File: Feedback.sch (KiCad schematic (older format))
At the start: 1 part

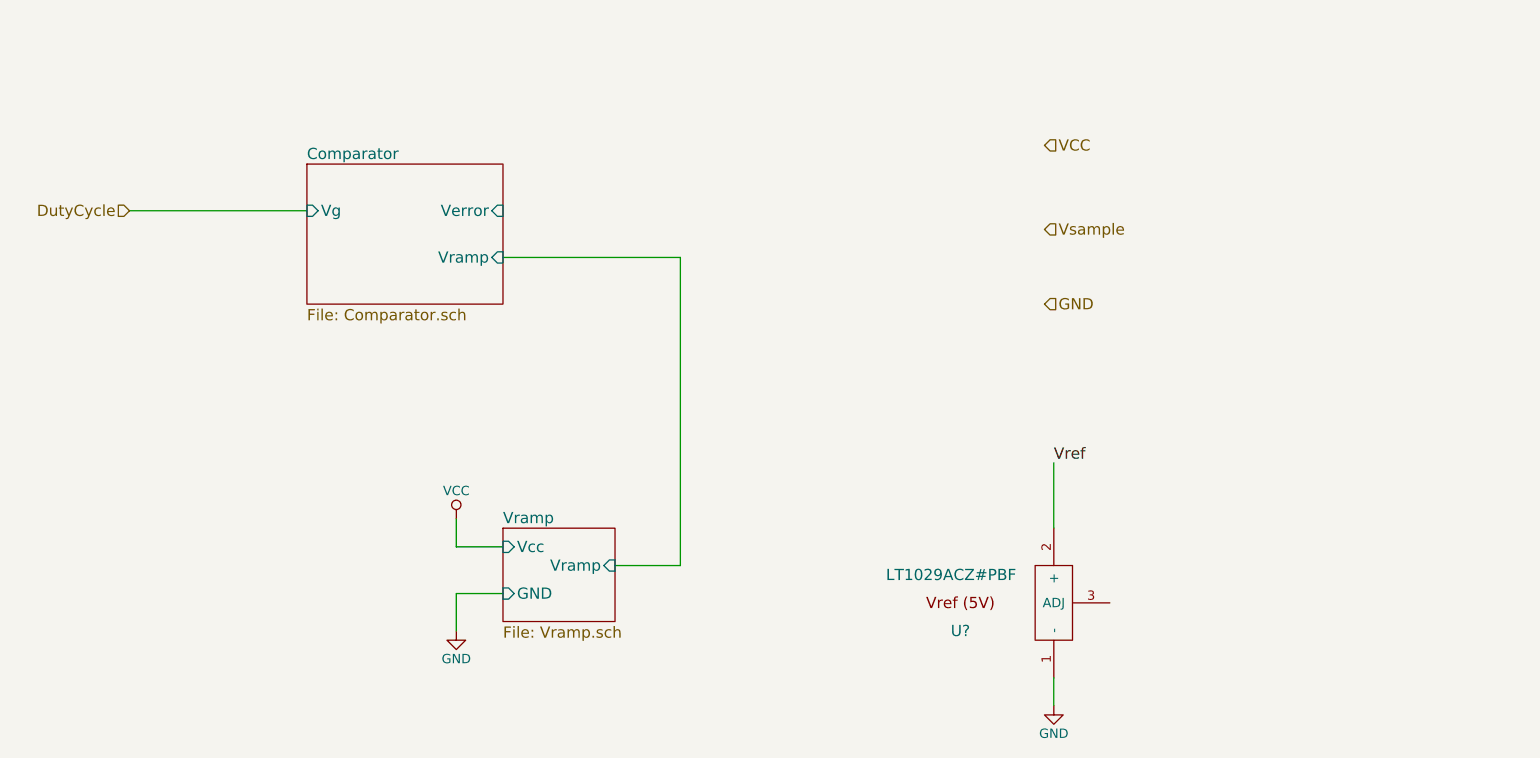
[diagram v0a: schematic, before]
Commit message: Added the basic Buck Schematic with the IRL2004
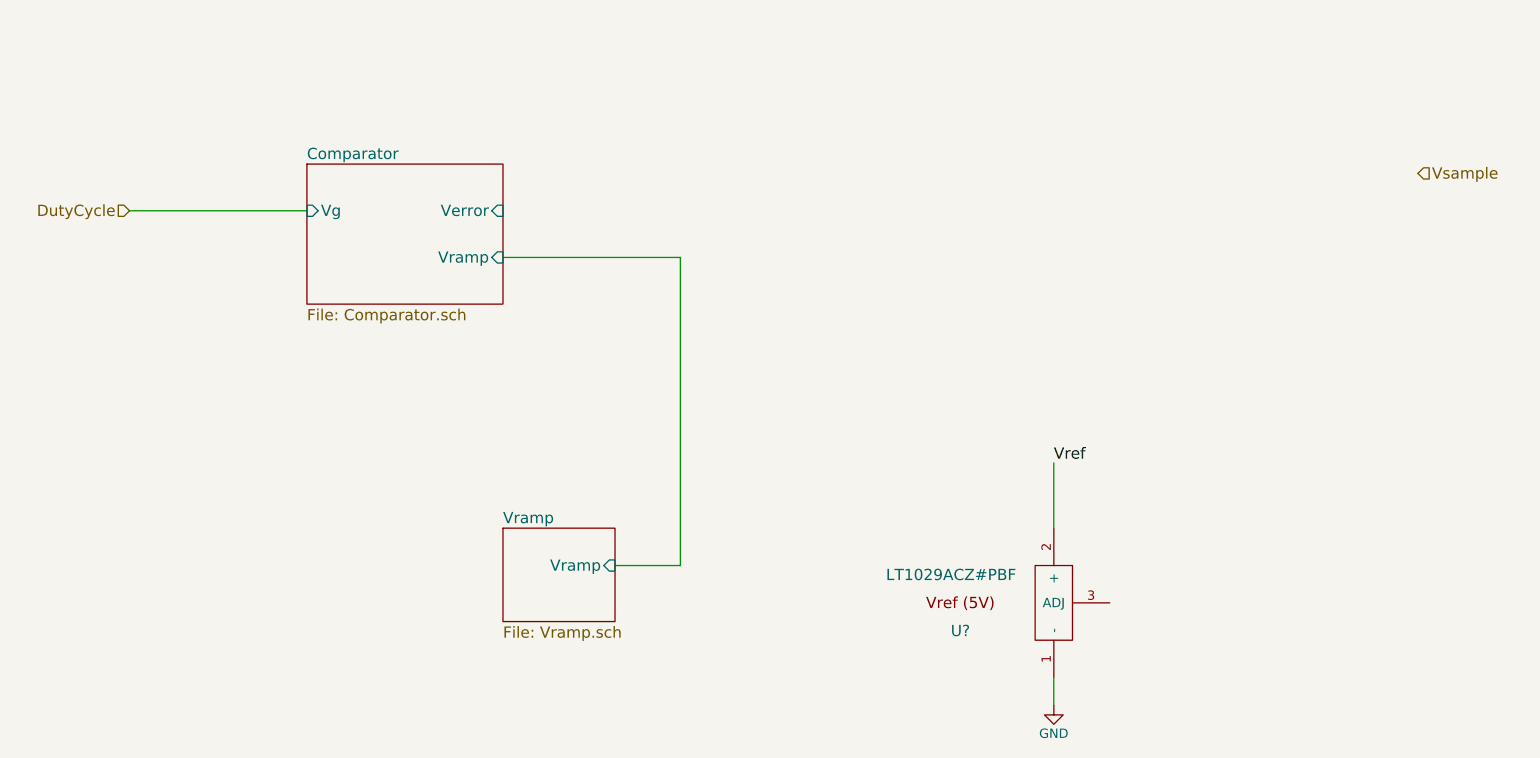
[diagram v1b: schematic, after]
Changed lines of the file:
@@
 LIBS:valves
 LIBS:Buck Supply-cache
+LIBS:ir
 EELAYER 25 0
 EELAYER END
@@
 Comment4 ""
 $EndDescr
-Text HLabel 6900 2800 2    60   Input ~ 0
+Text HLabel 8900 2500 2    60   Input ~ 0
 Vsample
 Text HLabel 2000 2700 0    60   Input ~ 0
@@
 F0 "Vramp" 60
 F1 "Vramp.sch" 60
-F2 "Vcc" I L 4000 4500 60
-F3 "GND" I L 4000 4750 60
-F4 "Vramp" I R 4600 4600 60
+F2 "Vramp" I R 4600 4600 60
 $EndSheet
-$Comp
-L GND #PWR?
-U 1 1 58B66F61
-P 3750 4950
-F 0 "#PWR?" H 3750 4700 50  0001 C CNN
-F 1 "GND" H 3750 4800 50  0000 C CNN
-F 2 "" H 3750 4950 50  0000 C CNN
-F 3 "" H 3750 4950 50  0000 C CNN
-	1    3750 4950
-	1    0    0    -1
-$EndComp
-$Comp
-L VCC #PWR?
-U 1 1 58B66F95
-P 3750 4350
-F 0 "#PWR?" H 3750 4200 50  0001 C CNN
-F 1 "VCC" H 3750 4500 50  0000 C CNN
-F 2 "" H 3750 4350 50  0000 C CNN
-F 3 "" H 3750 4350 50  0000 C CNN
-	1    3750 4350
-	1    0    0    -1
-$EndComp
-Wire Wire Line
-	4000 4500 3750 4500
-Wire Wire Line
-	3750 4500 3750 4350
-Wire Wire Line
-	3750 4950 3750 4750
-Wire Wire Line
-	3750 4750 4000 4750
 Wire Wire Line
 	4000 2950 4950 2950
@@
 Wire Wire Line
 	4950 4600 4600 4600
-Text HLabel 6900 3200 2    60   Input ~ 0
-GND
-Text HLabel 6900 2350 2    60   Input ~ 0
-VCC
 $EndSCHEMATC

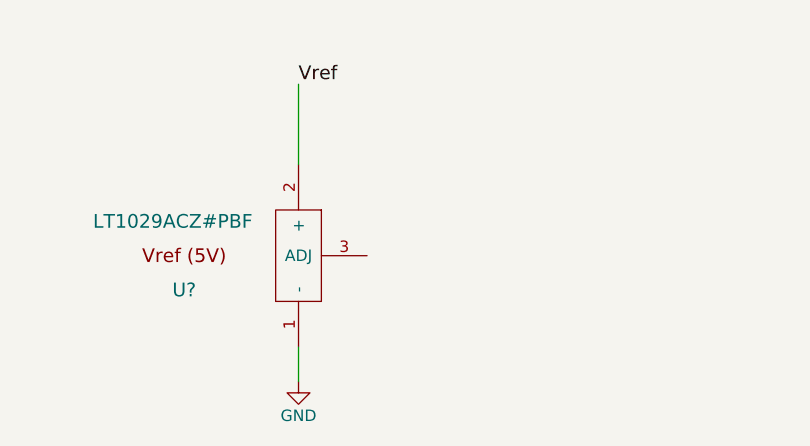
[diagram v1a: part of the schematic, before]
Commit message: Created Ramp Voltage Source
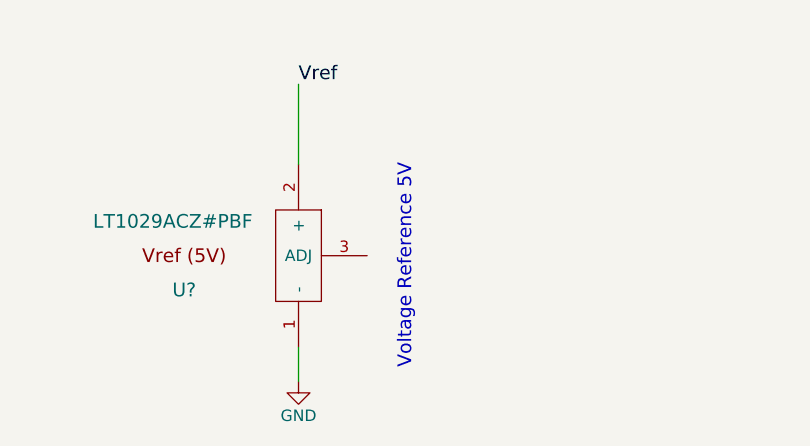
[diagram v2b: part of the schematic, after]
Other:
- note added: "Voltage Reference 5V\n"
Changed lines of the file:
@@
 Wire Wire Line
 	4950 4600 4600 4600
+Text Notes 7450 4400 3    60   ~ 0
+Voltage Reference 5V\n
 $EndSCHEMATC

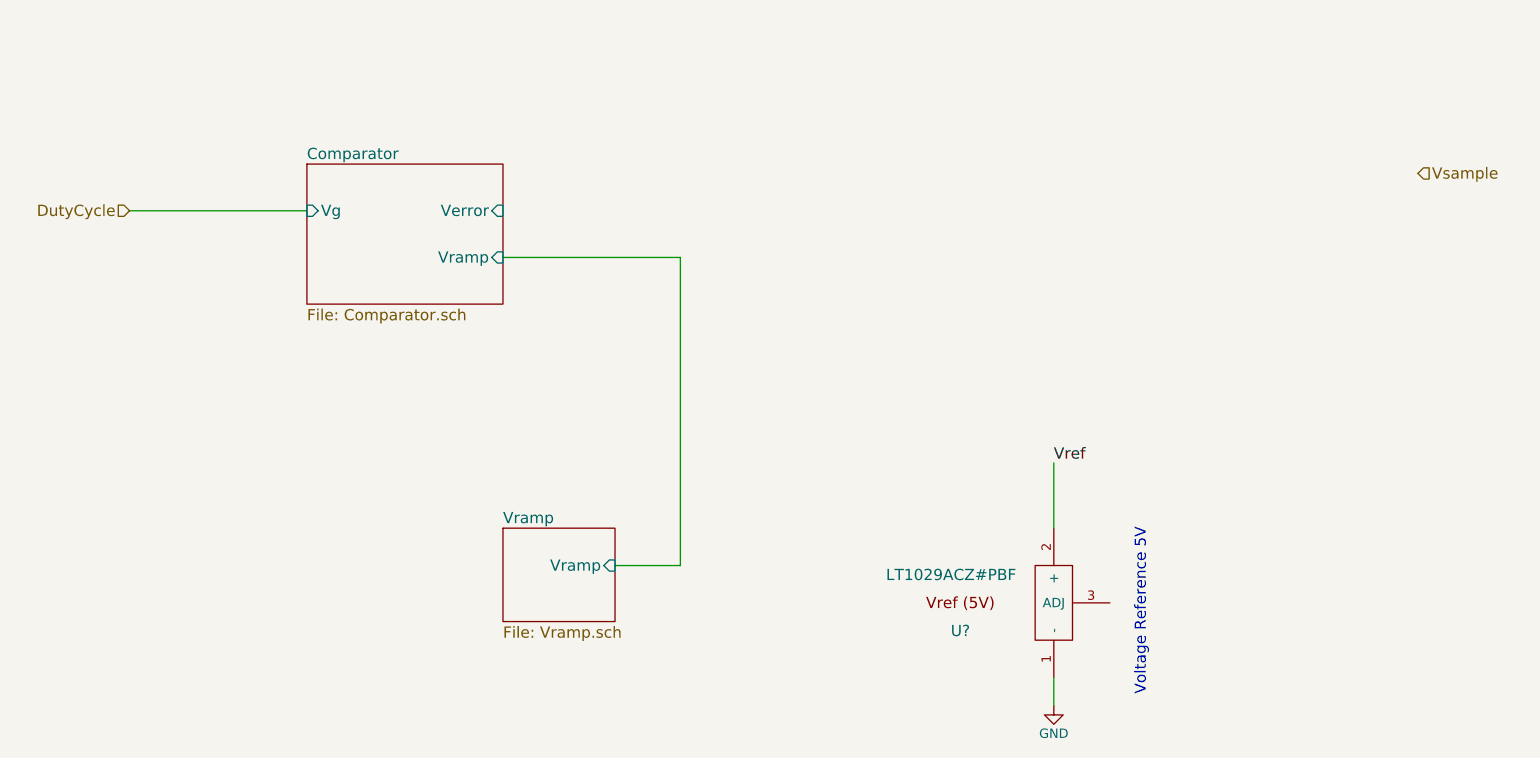
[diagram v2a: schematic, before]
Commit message: Finished the full circuit.
All thats left is to set the design parameters.
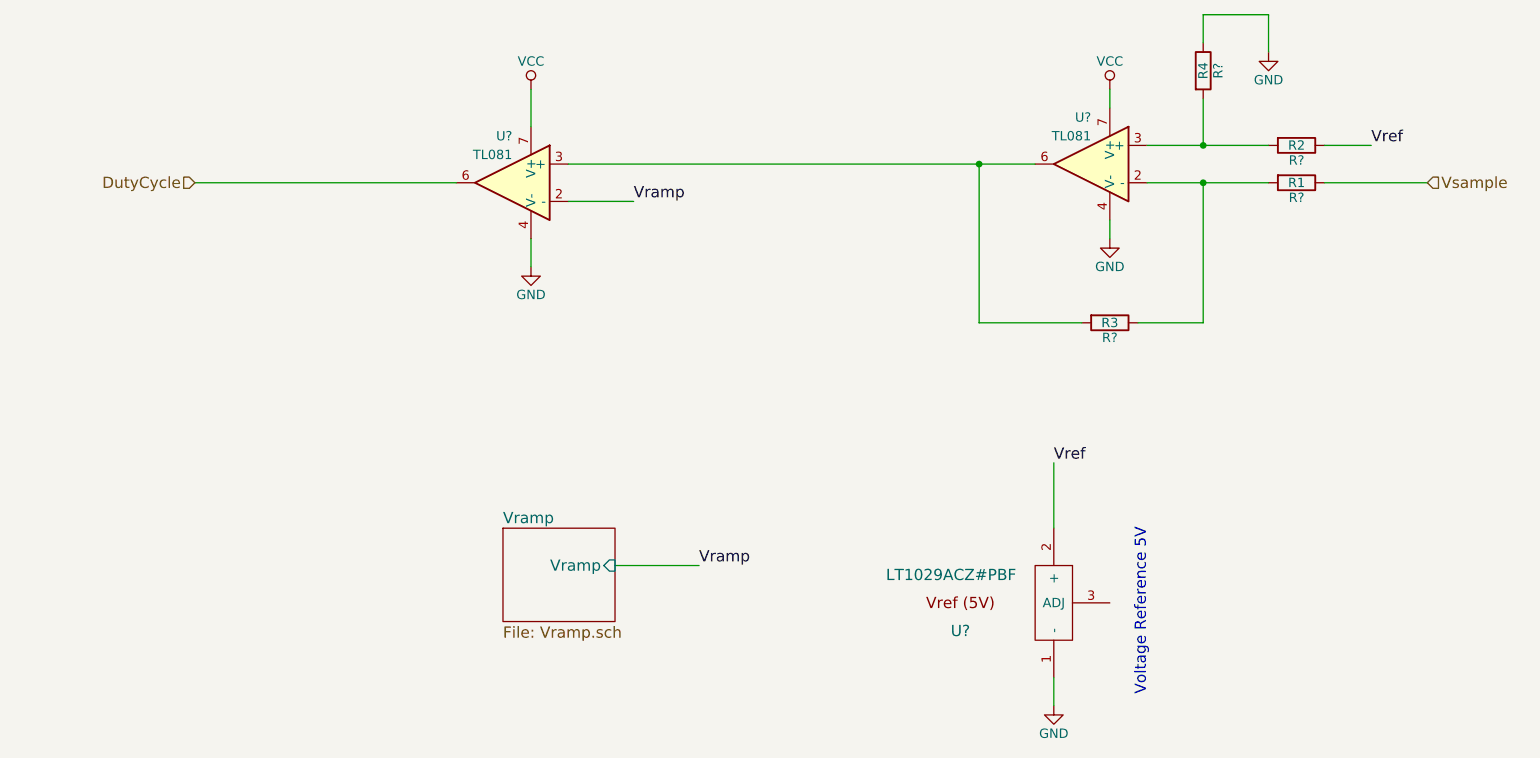
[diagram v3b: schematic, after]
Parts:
- added R?: R1, symbol R
- added R?: R3, symbol R
- added R?: R2, symbol R
- added R?: R4, symbol R
- added U? (x2): TL081, symbol TL081
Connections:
- net DutyCycle: now also U?.6
- net GND: now also R?.1, U?.4 (V-), U?.4 (V-)
- net Vref: now also R?.1
- net Vsample: now also R?.1
- new net: R?.1, R?.2, U?.2 (-)
- new net: R?.2, R?.2, U?.3 (+)
- new net: R?.2, U?.3 (+), U?.6
- new net VCC: U?.7 (V+), U?.7 (V+)
- new net Vramp: U?.2 (-)
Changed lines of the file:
@@
 $Descr A4 11693 8268
 encoding utf-8
-Sheet 2 5
+Sheet 2 4
 Title ""
 Date ""
@@
 Comment4 ""
 $EndDescr
-Text HLabel 8900 2500 2    60   Input ~ 0
+Text HLabel 8950 2550 2    60   Input ~ 0
 Vsample
-Text HLabel 2000 2700 0    60   Input ~ 0
+Text HLabel 2350 2550 0    60   Input ~ 0
 DutyCycle
-$Sheet
-S 2950 2450 1050 750
-U 58B64594
-F0 "Comparator" 60
-F1 "Comparator.sch" 60
-F2 "Vg" I L 2950 2700 60
-F3 "Verror" I R 4000 2700 60
-F4 "Vramp" I R 4000 2950 60
-$EndSheet
 $Comp
 L LT1029ACZ#PBF U?
@@
 Text Label 6950 4050 0    60   ~ 0
 Vref
-Wire Wire Line
-	2000 2700 2950 2700
 $Sheet
 S 4000 4400 600  500
@@
 F2 "Vramp" I R 4600 4600 60
 $EndSheet
-Wire Wire Line
-	4000 2950 4950 2950
-Wire Wire Line
-	4950 2950 4950 4600
-Wire Wire Line
-	4950 4600 4600 4600
 Text Notes 7450 4400 3    60   ~ 0
 Voltage Reference 5V\n
+$Comp
+L TL081 U?
+U 1 1 58B85FB5
+P 7150 2450
+F 0 "U?" H 7150 2700 50  0000 L CNN
+F 1 "TL081" H 7150 2600 50  0000 L CNN
+F 2 "" H 7200 2650 50  0000 C CNN
+F 3 "" H 7150 2700 50  0000 C CNN
+	1    7150 2450
+	-1   0    0    -1
+$EndComp
+Wire Wire Line
+	7450 2350 8100 2350
+Text Label 8650 2350 0    60   ~ 0
+Vref
+$Comp
+L GND #PWR?
+U 1 1 58B861EE
+P 7250 2850
+F 0 "#PWR?" H 7250 2600 50  0001 C CNN
+F 1 "GND" H 7250 2700 50  0000 C CNN
+F 2 "" H 7250 2850 50  0000 C CNN
+F 3 "" H 7250 2850 50  0000 C CNN
+	1    7250 2850
+	1    0    0    -1
+$EndComp
+Wire Wire Line
+	7250 2750 7250 2850
+$Comp
+L VCC #PWR?
+U 1 1 58B86218
+P 7250 2050
+F 0 "#PWR?" H 7250 1900 50  0001 C CNN
+F 1 "VCC" H 7250 2200 50  0000 C CNN
+F 2 "" H 7250 2050 50  0000 C CNN
+F 3 "" H 7250 2050 50  0000 C CNN
+	1    7250 2050
+	1    0    0    -1
+$EndComp
+Wire Wire Line
+	7250 2150 7250 2050
+$Comp
+L TL081 U?
+U 1 1 58B86315
+P 4050 2550
+F 0 "U?" H 4050 2800 50  0000 L CNN
+F 1 "TL081" H 4050 2700 50  0000 L CNN
+F 2 "" H 4100 2750 50  0000 C CNN
+F 3 "" H 4050 2800 50  0000 C CNN
+	1    4050 2550
+	-1   0    0    -1
+$EndComp
+$Comp
+L VCC #PWR?
+U 1 1 58B8636E
+P 4150 2050
+F 0 "#PWR?" H 4150 1900 50  0001 C CNN
+F 1 "VCC" H 4150 2200 50  0000 C CNN
+F 2 "" H 4150 2050 50  0000 C CNN
+F 3 "" H 4150 2050 50  0000 C CNN
+	1    4150 2050
+	1    0    0    -1
+$EndComp
+$Comp
+L GND #PWR?
+U 1 1 58B8638E
+P 4150 3000
+F 0 "#PWR?" H 4150 2750 50  0001 C CNN
+F 1 "GND" H 4150 2850 50  0000 C CNN
+F 2 "" H 4150 3000 50  0000 C CNN
+F 3 "" H 4150 3000 50  0000 C CNN
+	1    4150 3000
+	1    0    0    -1
+$EndComp
+Wire Wire Line
+	4150 2050 4150 2250
+Wire Wire Line
+	4150 3000 4150 2850
+Wire Wire Line
+	4350 2650 4700 2650
+Text Label 4700 2650 0    60   ~ 0
+Vramp
+Wire Wire Line
+	4600 4600 5050 4600
+Text Label 5050 4600 0    60   ~ 0
+Vramp
+Wire Wire Line
+	2350 2550 3750 2550
+$Comp
+L R R?
+U 1 1 58B87DD1
+P 8250 2550
+F 0 "R?" V 8330 2550 50  0000 C CNN
+F 1 "R1" V 8250 2550 50  0000 C CNN
+F 2 "" V 8180 2550 50  0000 C CNN
+F 3 "" H 8250 2550 50  0000 C CNN
+	1    8250 2550
+	0    1    1    0
+$EndComp
+$Comp
+L R R?
+U 1 1 58B87E2E
+P 7250 3300
+F 0 "R?" V 7330 3300 50  0000 C CNN
+F 1 "R3" V 7250 3300 50  0000 C CNN
+F 2 "" V 7180 3300 50  0000 C CNN
+F 3 "" H 7250 3300 50  0000 C CNN
+	1    7250 3300
+	0    1    1    0
+$EndComp
+Wire Wire Line
+	8400 2550 8950 2550
+Wire Wire Line
+	7450 2550 8100 2550
+Wire Wire Line
+	7400 3300 7750 3300
+Wire Wire Line
+	7750 3300 7750 2550
+Connection ~ 7750 2550
+Wire Wire Line
+	4350 2450 6850 2450
+Wire Wire Line
+	7100 3300 6550 3300
+Wire Wire Line
+	6550 3300 6550 2450
+Connection ~ 6550 2450
+$Comp
+L R R?
+U 1 1 58B880D8
+P 8250 2350
+F 0 "R?" V 8330 2350 50  0000 C CNN
+F 1 "R2" V 8250 2350 50  0000 C CNN
+F 2 "" V 8180 2350 50  0000 C CNN
+F 3 "" H 8250 2350 50  0000 C CNN
+	1    8250 2350
+	0    1    1    0
+$EndComp
+$Comp
+L R R?
+U 1 1 58B88123
+P 7750 1950
+F 0 "R?" V 7830 1950 50  0000 C CNN
+F 1 "R4" V 7750 1950 50  0000 C CNN
+F 2 "" V 7680 1950 50  0000 C CNN
+F 3 "" H 7750 1950 50  0000 C CNN
+	1    7750 1950
+	1    0    0    -1
+$EndComp
+Wire Wire Line
+	8650 2350 8400 2350
+Wire Wire Line
+	7750 2100 7750 2350
+Connection ~ 7750 2350
+$Comp
+L GND #PWR?
+U 1 1 58B88206
+P 8100 1850
+F 0 "#PWR?" H 8100 1600 50  0001 C CNN
+F 1 "GND" H 8100 1700 50  0000 C CNN
+F 2 "" H 8100 1850 50  0000 C CNN
+F 3 "" H 8100 1850 50  0000 C CNN
+	1    8100 1850
+	1    0    0    -1
+$EndComp
+Wire Wire Line
+	7750 1800 7750 1650
+Wire Wire Line
+	7750 1650 8100 1650
+Wire Wire Line
+	8100 1650 8100 1850
 $EndSCHEMATC

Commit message: Did a whole bunch of layout
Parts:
- R2, R3, R4, R5: renamed from R?; footprint (none) -> Resistors_THT:Resistor_Horizontal_RM7mm
- U1, U3: renamed from U?; footprint (none) -> Housings_DIP:DIP-8_W7.62mm_LongPads
- U2: renamed from U?; footprint (none) -> TO_SOT_Packages_THT:TO-92_Inline_Wide
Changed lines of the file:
@@
 DutyCycle
 $Comp
-L LT1029ACZ#PBF U?
+L LT1029ACZ#PBF U2
 U 1 1 58B64C1F
 P 6950 4900
-F 0 "U?" H 6450 4850 60  0000 C CNN
+F 0 "U2" H 6450 4850 60  0000 C CNN
 F 1 "LT1029ACZ#PBF" H 6400 5150 60  0000 C CNN
-F 2 "" H 6950 4900 60  0000 C CNN
+F 2 "TO_SOT_Packages_THT:TO-92_Inline_Wide" H 6950 4900 60  0001 C CNN
 F 3 "" H 6950 4900 60  0000 C CNN
 	1    6950 4900
@@
 $EndComp
 $Comp
-L GND #PWR?
+L GND #PWR06
 U 1 1 58B64C4A
 P 6950 5350
-F 0 "#PWR?" H 6950 5100 50  0001 C CNN
+F 0 "#PWR06" H 6950 5100 50  0001 C CNN
 F 1 "GND" H 6950 5200 50  0000 C CNN
 F 2 "" H 6950 5350 50  0000 C CNN
@@
 Voltage Reference 5V\n
 $Comp
-L TL081 U?
+L TL081 U3
 U 1 1 58B85FB5
 P 7150 2450
-F 0 "U?" H 7150 2700 50  0000 L CNN
+F 0 "U3" H 7150 2700 50  0000 L CNN
 F 1 "TL081" H 7150 2600 50  0000 L CNN
-F 2 "" H 7200 2650 50  0000 C CNN
+F 2 "Housings_DIP:DIP-8_W7.62mm_LongPads" H 7200 2650 50  0001 C CNN
 F 3 "" H 7150 2700 50  0000 C CNN
 	1    7150 2450
@@
 Vref
 $Comp
-L GND #PWR?
+L GND #PWR07
 U 1 1 58B861EE
 P 7250 2850
-F 0 "#PWR?" H 7250 2600 50  0001 C CNN
+F 0 "#PWR07" H 7250 2600 50  0001 C CNN
 F 1 "GND" H 7250 2700 50  0000 C CNN
 F 2 "" H 7250 2850 50  0000 C CNN
@@
 	7250 2750 7250 2850
 $Comp
-L VCC #PWR?
+L VCC #PWR08
 U 1 1 58B86218
 P 7250 2050
-F 0 "#PWR?" H 7250 1900 50  0001 C CNN
+F 0 "#PWR08" H 7250 1900 50  0001 C CNN
 F 1 "VCC" H 7250 2200 50  0000 C CNN
 F 2 "" H 7250 2050 50  0000 C CNN
@@
 	7250 2150 7250 2050
 $Comp
-L TL081 U?
+L TL081 U1
 U 1 1 58B86315
 P 4050 2550
-F 0 "U?" H 4050 2800 50  0000 L CNN
+F 0 "U1" H 4050 2800 50  0000 L CNN
 F 1 "TL081" H 4050 2700 50  0000 L CNN
-F 2 "" H 4100 2750 50  0000 C CNN
+F 2 "Housings_DIP:DIP-8_W7.62mm_LongPads" H 4100 2750 50  0001 C CNN
 F 3 "" H 4050 2800 50  0000 C CNN
 	1    4050 2550
@@
 $EndComp
 $Comp
-L VCC #PWR?
+L VCC #PWR09
 U 1 1 58B8636E
 P 4150 2050
-F 0 "#PWR?" H 4150 1900 50  0001 C CNN
+F 0 "#PWR09" H 4150 1900 50  0001 C CNN
 F 1 "VCC" H 4150 2200 50  0000 C CNN
 F 2 "" H 4150 2050 50  0000 C CNN
@@
 $EndComp
 $Comp
-L GND #PWR?
+L GND #PWR010
 U 1 1 58B8638E
 P 4150 3000
-F 0 "#PWR?" H 4150 2750 50  0001 C CNN
+F 0 "#PWR010" H 4150 2750 50  0001 C CNN
 F 1 "GND" H 4150 2850 50  0000 C CNN
 F 2 "" H 4150 3000 50  0000 C CNN
@@
 	2350 2550 3750 2550
 $Comp
-L R R?
+L R R5
 U 1 1 58B87DD1
 P 8250 2550
-F 0 "R?" V 8330 2550 50  0000 C CNN
+F 0 "R5" V 8330 2550 50  0000 C CNN
 F 1 "R1" V 8250 2550 50  0000 C CNN
-F 2 "" V 8180 2550 50  0000 C CNN
+F 2 "Resistors_THT:Resistor_Horizontal_RM7mm" V 8180 2550 50  0001 C CNN
 F 3 "" H 8250 2550 50  0000 C CNN
 	1    8250 2550
@@
 $EndComp
 $Comp
-L R R?
+L R R2
 U 1 1 58B87E2E
 P 7250 3300
-F 0 "R?" V 7330 3300 50  0000 C CNN
+F 0 "R2" V 7330 3300 50  0000 C CNN
 F 1 "R3" V 7250 3300 50  0000 C CNN
-F 2 "" V 7180 3300 50  0000 C CNN
+F 2 "Resistors_THT:Resistor_Horizontal_RM7mm" V 7180 3300 50  0001 C CNN
 F 3 "" H 7250 3300 50  0000 C CNN
 	1    7250 3300
@@
 Connection ~ 6550 2450
 $Comp
-L R R?
+L R R4
 U 1 1 58B880D8
 P 8250 2350
-F 0 "R?" V 8330 2350 50  0000 C CNN
+F 0 "R4" V 8330 2350 50  0000 C CNN
 F 1 "R2" V 8250 2350 50  0000 C CNN
-F 2 "" V 8180 2350 50  0000 C CNN
+F 2 "Resistors_THT:Resistor_Horizontal_RM7mm" V 8180 2350 50  0001 C CNN
 F 3 "" H 8250 2350 50  0000 C CNN
 	1    8250 2350
@@
 $EndComp
 $Comp
-L R R?
+L R R3
 U 1 1 58B88123
 P 7750 1950
-F 0 "R?" V 7830 1950 50  0000 C CNN
+F 0 "R3" V 7830 1950 50  0000 C CNN
 F 1 "R4" V 7750 1950 50  0000 C CNN
-F 2 "" V 7680 1950 50  0000 C CNN
+F 2 "Resistors_THT:Resistor_Horizontal_RM7mm" V 7680 1950 50  0001 C CNN
 F 3 "" H 7750 1950 50  0000 C CNN
 	1    7750 1950
@@
 Connection ~ 7750 2350
 $Comp
-L GND #PWR?
+L GND #PWR011
 U 1 1 58B88206
 P 8100 1850
-F 0 "#PWR?" H 8100 1600 50  0001 C CNN
+F 0 "#PWR011" H 8100 1600 50  0001 C CNN
 F 1 "GND" H 8100 1700 50  0000 C CNN
 F 2 "" H 8100 1850 50  0000 C CNN
